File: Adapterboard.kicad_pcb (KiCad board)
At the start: 2 copper layers, 100 x 100 mm, 72 parts, among them J101 1xPin, J102 1xPin, J103 JTAG(optional), J104 1xPin, J105 TUNNEL_IN, J106 Power in +15V, J107 Power in -15V, J108 Power out Preamplifier, J109 Piezo, J110 2xPin, J111 USB_Connector, U101 ADS1115A(optional), U102 DAC X, U103 ESP32-DEVKITC-32D, U104 DAC Y, U106 DAC Z, U107 ADC 8 Click, U108 mint, U109 UniRegensburg, U110 OTH, U201 TL072, U301 TL072

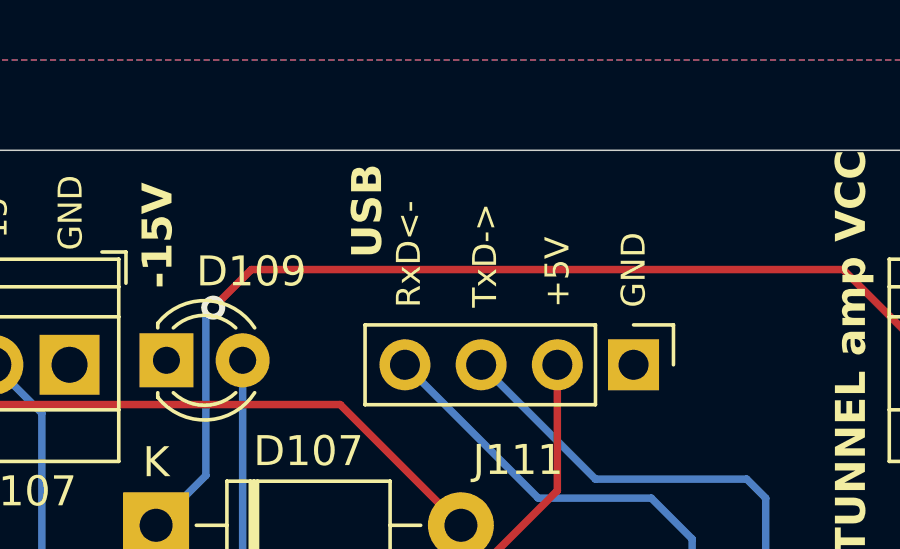
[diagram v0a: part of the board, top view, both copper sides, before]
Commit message: Rx and Tx have been swapped. New Gerber files have been generated. Version number updated to 3.0.1 on gerber silkscreen file
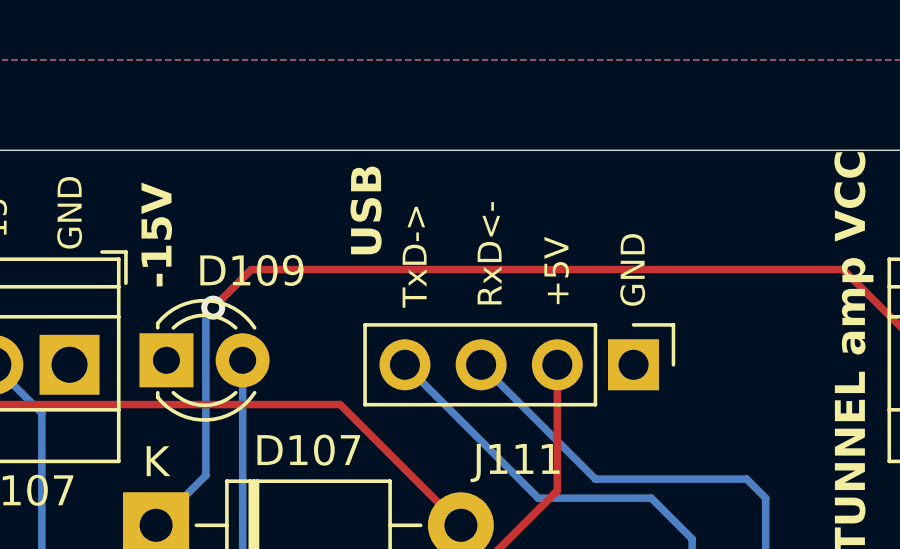
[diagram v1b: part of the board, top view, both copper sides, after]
